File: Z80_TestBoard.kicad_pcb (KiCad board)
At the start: 2 copper layers, 68.5 x 58 mm, 23 parts, among them J1 ICSP, J2 UART, J3 I2C, J5 CLK_SW, J6 M1_O, J7 USB_B_Mini, U1 Z84C00_PLCC, U2 PIC18F4520-xP, Y2 Crystal, Y3 CXO_DIP8

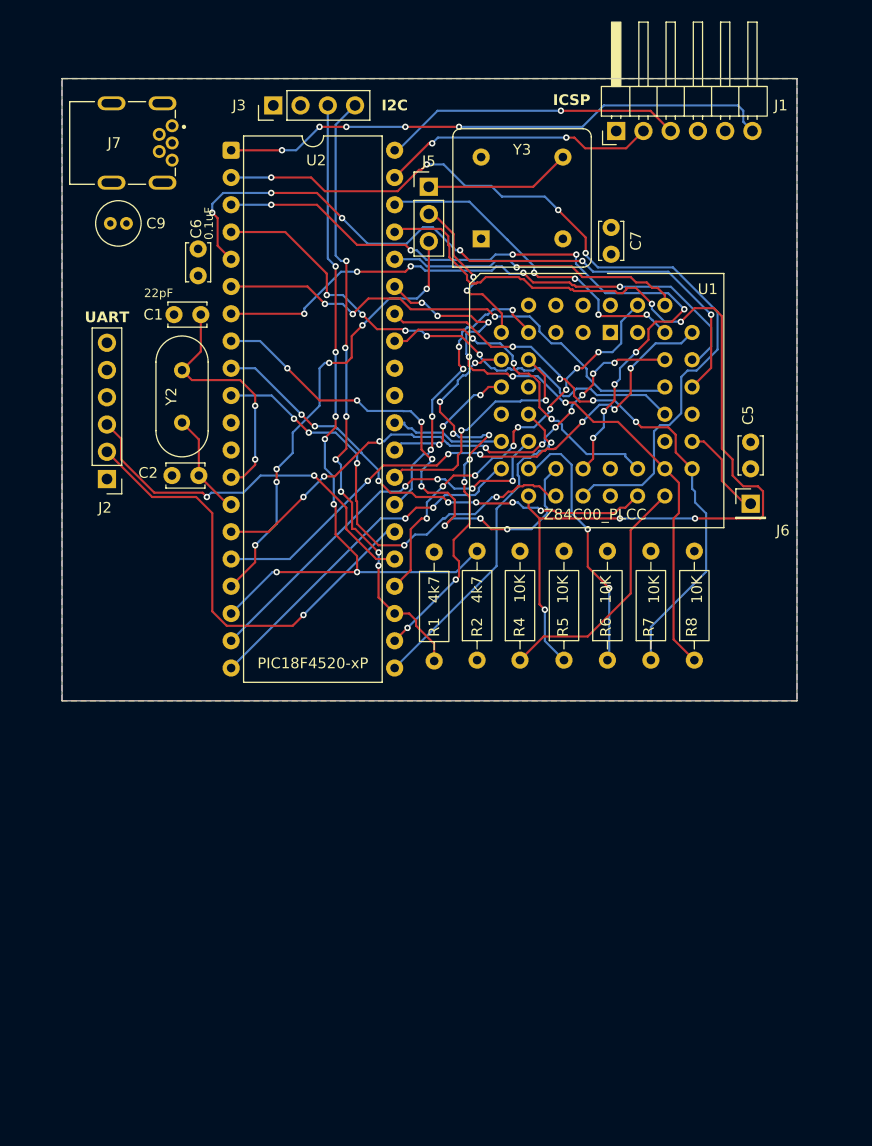
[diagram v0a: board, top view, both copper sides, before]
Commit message: Refine with NE555P + LED.
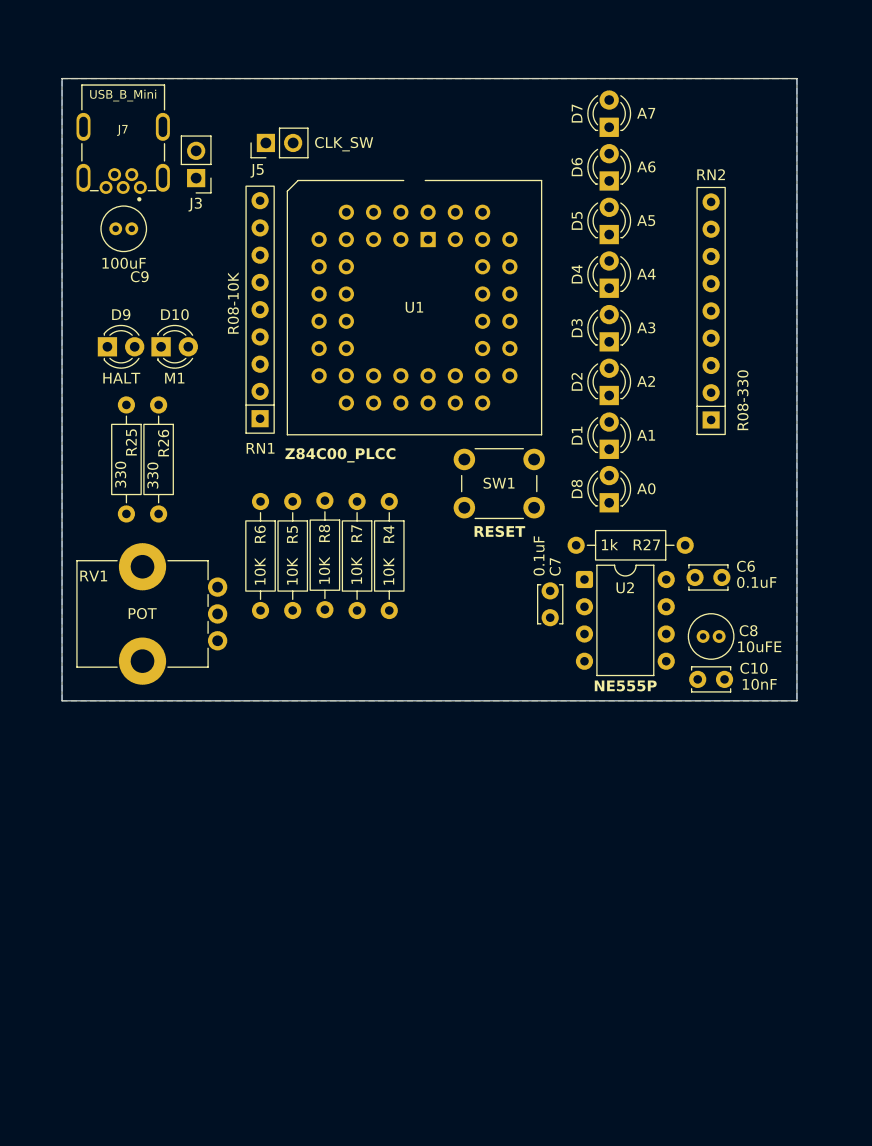
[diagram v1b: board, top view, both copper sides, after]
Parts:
- removed C1, C2: 22pF, Capacitor_THT:C_Disc_D3.4mm_W2.1mm_P2.50mm
- removed C5: 0.1uF, Capacitor_THT:C_Disc_D3.4mm_W2.1mm_P2.50mm
- removed J1: ICSP, Connector_PinHeader_2.54mm:PinHeader_1x06_P2.54mm_Horizontal
- removed J2: UART, Connector_PinHeader_2.54mm:PinHeader_1x06_P2.54mm_Vertical
- removed J6: M1_O, Connector_PinHeader_2.54mm:PinHeader_1x01_P2.54mm_Vertical
- removed R1, R2: 4k7, Resistor_THT:R_Axial_DIN0207_L6.3mm_D2.5mm_P10.16mm_Horizontal
- removed Y2: Crystal, Crystal:Crystal_HC49-4H_Vertical
- removed Y3: CXO_DIP8, Oscillator:Oscillator_DIP-8
- added C10: 10nF, Capacitor_THT:C_Disc_D3.4mm_W2.1mm_P2.50mm, F.Cu at (173.2, 110.0)
- added C8: 10uFE, Capacitor_THT:C_Radial_D4.0mm_H5.0mm_P1.50mm, F.Cu at (171.2, 106.0)
- added D1: A1, LED_THT:LED_D3.0mm, F.Cu at (162.5, 88.6)
- added D10: M1, LED_THT:LED_D3.0mm, F.Cu at (120.7, 79.0)
- added D2: A2, LED_THT:LED_D3.0mm, F.Cu at (162.5, 83.5)
- added D3: A3, LED_THT:LED_D3.0mm, F.Cu at (162.5, 78.5)
- added D4: A4, LED_THT:LED_D3.0mm, F.Cu at (162.5, 73.5)
- added D5: A5, LED_THT:LED_D3.0mm, F.Cu at (162.5, 68.5)
- added D6: A6, LED_THT:LED_D3.0mm, F.Cu at (162.5, 63.5)
- added D7: A7, LED_THT:LED_D3.0mm, F.Cu at (162.5, 58.5)
- added D8: A0, LED_THT:LED_D3.0mm, F.Cu at (162.5, 93.5)
- added D9: HALT, LED_THT:LED_D3.0mm, F.Cu at (115.7, 79.0)
- added R25: 330, Resistor_THT:R_Axial_DIN0207_L6.3mm_D2.5mm_P10.16mm_Horizontal, F.Cu at (117.5, 84.4)
- added R26: 330, Resistor_THT:R_Axial_DIN0207_L6.3mm_D2.5mm_P10.16mm_Horizontal, F.Cu at (120.5, 84.4)
- added R27: 1k, Resistor_THT:R_Axial_DIN0207_L6.3mm_D2.5mm_P10.16mm_Horizontal, F.Cu at (169.6, 97.5)
- added RN1: R08-10K, Resistor_THT:R_Array_SIP9, F.Cu at (130.0, 85.7)
- added RN2: R08-330, Resistor_THT:R_Array_SIP9, F.Cu at (172.0, 85.8)
- added RV1: POT, Potentiometer_THT:Potentiometer_Bourns_PTV09A-1_Single_Vertical, F.Cu at (126.0, 101.4)
- added SW1: RESET, Button_Switch_THT:SW_PUSH_6mm, F.Cu at (149.0, 89.5)
- J3: value I2C -> PWR; footprint Connector_PinHeader_2.54mm:PinHeader_1x04_P2.54mm_Vertical -> Connector_PinHeader_2.54mm:PinHeader_1x02_P2.54mm_Vertical
- J5: footprint Connector_PinHeader_2.54mm:PinHeader_1x03_P2.54mm_Vertical -> Connector_PinHeader_2.54mm:PinHeader_1x02_P2.54mm_Vertical
- U2: value PIC18F4520-xP -> NE555P; footprint Package_DIP:DIP-40_W15.24mm -> Package_DIP:DIP-8_W7.62mm
- moved C6 55.5 mm to (170.5, 100.5), turned to 0 degrees
- moved U2 51.8 mm to (160.2, 100.7)
- moved R8 37.5 mm to (136.0, 93.3), turned to -90 degrees
- moved R6 35.6 mm to (130.0, 93.4), turned to -90 degrees
- moved C7 34.3 mm to (157.0, 101.8)
- moved R7 31.1 mm to (139.0, 93.4), turned to -90 degrees
- moved R5 29.3 mm to (133.0, 93.4), turned to -90 degrees
- moved R4 19.2 mm to (142.0, 93.4), turned to -90 degrees
- moved U1 19.1 mm to (145.6, 69.0)
- moved J5 15.7 mm to (130.5, 60.0), turned to 90 degrees
- moved J3 9.88 mm to (124.0, 63.3), turned to 180 degrees
- moved J7 4.90 mm to (117.2, 63.2), turned to 0 degrees
- moved C9 0.71 mm to (116.5, 68.0)
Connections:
- J5 pad 1: /OSC_CLK -> /555_CLK
- U1 pad 21: /MREQ -> unconnected-(U1-~{MREQ}-Pad21)
- U1 pad 22: /IORQ -> unconnected-(U1-~{IORQ}-Pad22)
- U1 pad 23: /RD -> unconnected-(U1-~{RD}-Pad23)
- U1 pad 26: /WR -> unconnected-(U1-~{WR}-Pad26)
- U1 pad 27: /BUSACK -> unconnected-(U1-~{BUSACK}-Pad27)
- U1 pad 32: /RFSH -> unconnected-(U1-~{RFSH}-Pad32)
- U1 pad 42: /A8 -> unconnected-(U1-A_{8}-Pad42)
- U2 pad 1: /MCLR -> GND
- U2 pad 2: /IORQ -> Net-(U2-THRES)
- U2 pad 3: /RD -> /555_CLK
- U2 pad 4: /A0 -> VCC
- U2 pad 5: /A1 -> Net-(U2-CONT)
- U2 pad 6: /A2 -> Net-(U2-THRES)
- U2 pad 7: /A3 -> Net-(U2-DISCH)
- U2 pad 8: /MREQ -> VCC
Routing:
- net /INT: track 96.3 -> 0.00 mm, vias 5 -> 0
- net /IORQ: track 79.6 -> 0.00 mm, vias 4 -> 0
- net /SCL: track 70.5 -> 0.00 mm, vias 7 -> 0
- net /RD: track 66.9 -> 0.00 mm, vias 9 -> 0
- net /A1: track 66.3 -> 0.00 mm, vias 6 -> 0
- net /SDA: track 58.5 -> 0.00 mm, vias 7 -> 0
- net /RESET: track 57.4 -> 0.00 mm, vias 6 -> 0
- net /BUSREQ: track 55.9 -> 0.00 mm, vias 4 -> 0
- net /A5: track 53.8 -> 0.00 mm, vias 6 -> 0
- net /A3: track 53.7 -> 0.00 mm, vias 5 -> 0
- net /MCLR: track 51.9 -> 0.00 mm, vias 5 -> 0
- net /A0: track 50.0 -> 0.00 mm, vias 5 -> 0
- net /MREQ: track 49.7 -> 0.00 mm, vias 8 -> 0
- net /A4: track 49.6 -> 0.00 mm, vias 10 -> 0
- net /A2: track 46.5 -> 0.00 mm, vias 3 -> 0
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- removed copper zone on F.Cu, net VCC

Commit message: finish routing/layout.
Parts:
- RV1: value POT -> 100K-POT
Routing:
- net /555_CLK: track 0.00 -> 73.9 mm, vias 0 -> 3
- net Net-(U2-DISCH): track 0.00 -> 50.4 mm, vias 0 -> 4
- net Net-(U2-THRES): track 0.00 -> 48.8 mm, vias 0 -> 2
- net /RESET: track 0.00 -> 35.3 mm
- net /HALT: track 0.00 -> 31.2 mm, vias 0 -> 1
- net /M1: track 0.00 -> 30.9 mm, vias 0 -> 2
- net /A7: track 0.00 -> 21.2 mm, vias 0 -> 2
- net /A0: track 0.00 -> 20.4 mm, vias 0 -> 2
- net /BUSREQ: track 0.00 -> 20.2 mm, vias 0 -> 2
- net /A1: track 0.00 -> 16.6 mm, vias 0 -> 2
- net /D7: track 0.00 -> 16.5 mm, vias 0 -> 2
- net /D6: track 0.00 -> 16.0 mm, vias 0 -> 1
- net /D5: track 0.00 -> 15.5 mm, vias 0 -> 2
- net /A2: track 0.00 -> 15.5 mm, vias 0 -> 2
- net /NMI: track 0.00 -> 15.0 mm
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- added copper zone on F.Cu, net VCC

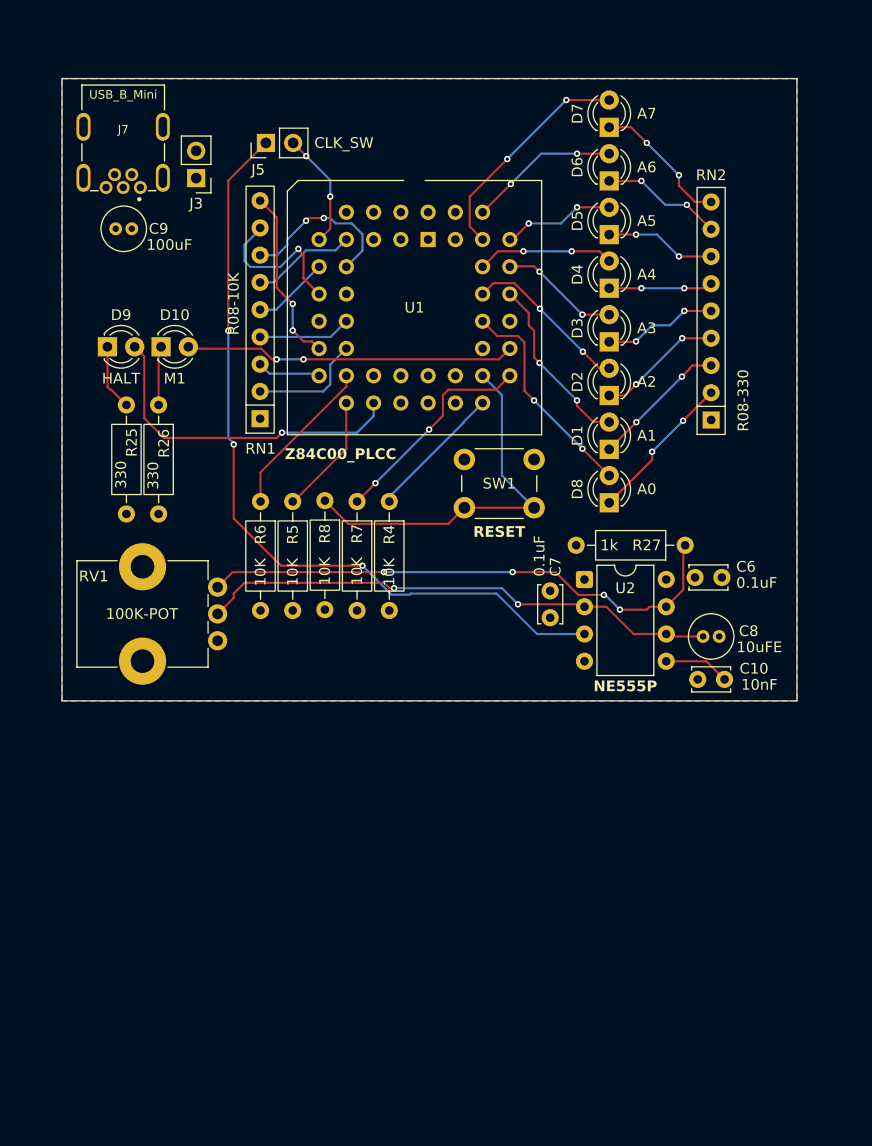
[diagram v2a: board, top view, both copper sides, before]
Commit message: add SOP28-DIP28 + LED-Board.
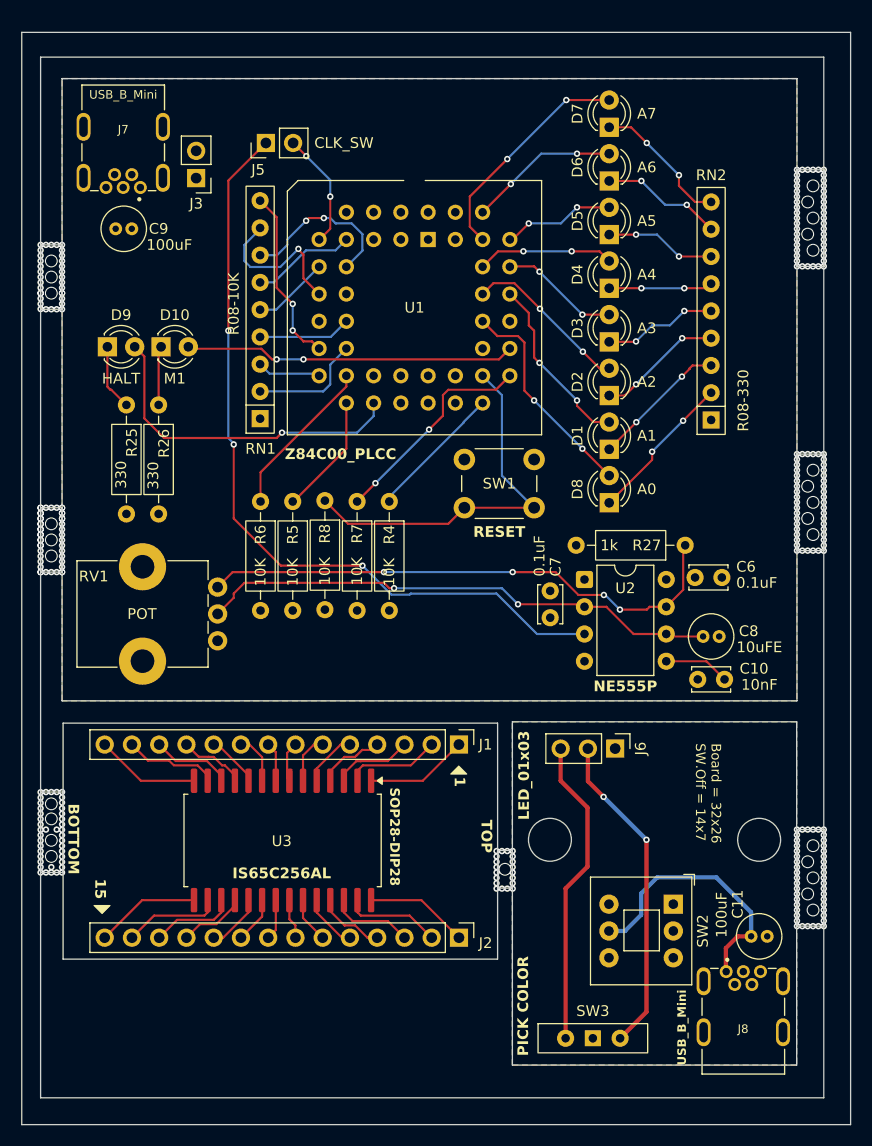
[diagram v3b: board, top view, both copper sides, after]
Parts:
- added C11: 100uF, Capacitor_THT:C_Radial_D4.0mm_H5.0mm_P1.50mm, F.Cu at (177.2, 133.9)
- added J1: LEFT, Connector_PinHeader_2.54mm:PinHeader_1x14_P2.54mm_Vertical, F.Cu at (148.5, 116.1)
- added J2: RIGHT, Connector_PinHeader_2.54mm:PinHeader_1x14_P2.54mm_Vertical, F.Cu at (148.5, 134.1)
- added J6: LED_01x03, Connector_PinHeader_2.54mm:PinHeader_1x03_P2.54mm_Vertical, F.Cu at (163.1, 116.5)
- added J8: USB_B_Mini, Connector_USB:USB_MINI_B_90_Angled, F.Cu at (175.0, 138.1)
- added SW2: ON|OFF, Button_Switch_THT:SW_Push_2P2T_Toggle_CK_PVA2OAH5xxxxxxV2, F.Cu at (168.5, 130.9)
- added SW3: PICK COLOR, Button_Switch_THT:SW_Slide-03_Wuerth-WS-SLTV_10x2.5x6.4_P2.54mm, F.Cu at (161.0, 143.4)
- added U3: IS65C256AL, Package_SO:SOP-28_8.4x18.16mm_P1.27mm, F.Cu at (132.1, 125.0)
- RV1: value 100K-POT -> POT
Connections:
- net /555_CLK renamed /Root/555_CLK
- net /A0 renamed /Root/A0
- net /A1 renamed /Root/A1
- net /A2 renamed /Root/A2
- net /A3 renamed /Root/A3
- net /A4 renamed /Root/A4
- net /A5 renamed /Root/A5
- net /A6 renamed /Root/A6
- net /A7 renamed /Root/A7
- net /BUSREQ renamed /Root/BUSREQ
- net /D0 renamed /Root/D0
- net /D1 renamed /Root/D1
- net /D2 renamed /Root/D2
- net /D3 renamed /Root/D3
- net /D4 renamed /Root/D4
- net /D5 renamed /Root/D5
- net /D6 renamed /Root/D6
- net /D7 renamed /Root/D7
- net /HALT renamed /Root/HALT
- net /INT renamed /Root/INT
- net /M1 renamed /Root/M1
- net /NMI renamed /Root/NMI
- net /RESET renamed /Root/RESET
- net /WAIT renamed /Root/WAIT
- net /Z80_CLK renamed /Root/Z80_CLK
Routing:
- net /LED_Board/LED_V1-: track 0.00 -> 30.3 mm, vias 0 -> 2
- net /LED_Board/LED_V2-: track 0.00 -> 28.9 mm
- net Net-(J8-VBUS): track 0.00 -> 25.0 mm
- net /SOP28-DIP28/IO_3: track 0.00 -> 9.77 mm
- net /SOP28-DIP28/GND3: track 0.00 -> 9.72 mm
- net /SOP28-DIP28/VCC3: track 0.00 -> 9.63 mm
- net /SOP28-DIP28/A14: track 0.00 -> 9.58 mm
- net /SOP28-DIP28/IO_4: track 0.00 -> 9.17 mm
- net /SOP28-DIP28/WE: track 0.00 -> 9.03 mm
- net /SOP28-DIP28/A12: track 0.00 -> 8.86 mm
- net /SOP28-DIP28/IO_2: track 0.00 -> 8.75 mm
- net /SOP28-DIP28/IO_5: track 0.00 -> 7.90 mm
- net /SOP28-DIP28/A13: track 0.00 -> 7.76 mm
- net /SOP28-DIP28/IO_1: track 0.00 -> 7.48 mm
- net /SOP28-DIP28/A7: track 0.00 -> 7.44 mm
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- added copper zone on B.Cu, net GND1
- added copper zone on F.Cu, net VCCQ
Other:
- board size 68.5 x 58 mm -> 77.3 x 101.8 mm
- board text added: "1"
- board text added: "15"
- board text added: "BOTTOM"
- board text added: "Board = 32x26 SW.Off = 14x7"
- board text added: "SOP28-DIP28"
- board text added: "TOP"
